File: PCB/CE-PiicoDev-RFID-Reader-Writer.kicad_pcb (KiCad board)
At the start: 2 copper layers, 25.4 x 52 mm, 63 parts, among them J1 , J2 , J3 Conn_01x06_Male, J4 Conn_01x01_Male, SW1 SW_DIP_x02, U1 MFRC522, Y1 27.12MHz 12pF

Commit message: v10 Release
Remove testpoints
Change ASW order so SW1 is LSB
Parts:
- removed TP1, TP2, TP3, TP4: TestPoint, CoreElectronics_Components:TestPoint_Pad_0.7x0.7mm
- moved R6 0.10 mm to (95.9, 109.8)
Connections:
- U1 pad 29: Net-(R7-Pad1) -> Net-(R6-Pad1)
- U1 pad 30: Net-(R6-Pad1) -> Net-(R7-Pad1)
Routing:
- net Net-(C3-Pad2): track 6.82 -> 4.16 mm, vias 1 -> 0
- net Net-(L2-Pad1): track 10.6 -> 8.78 mm, vias 3 -> 2
- net GND: track 35.1 -> 36.5 mm
- net Net-(R7-Pad1): track 16.7 -> 18.0 mm
- net Net-(C2-Pad2): track 7.86 -> 6.73 mm, vias 1 -> 0
- net Net-(L1-Pad1): vias 1 -> 0
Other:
- board text added: "0x2C 0x2D 0x2E 0x2F"
- board text added: "1 OFF ON OFF ON"
- board text added: "2 OFF OFF ON ON"
- board text added: "ASW"
- board text added: "RFID Module"
- board text added: "v10"
- board text removed: "RFID Reader Writer"
- board text removed: "v04"

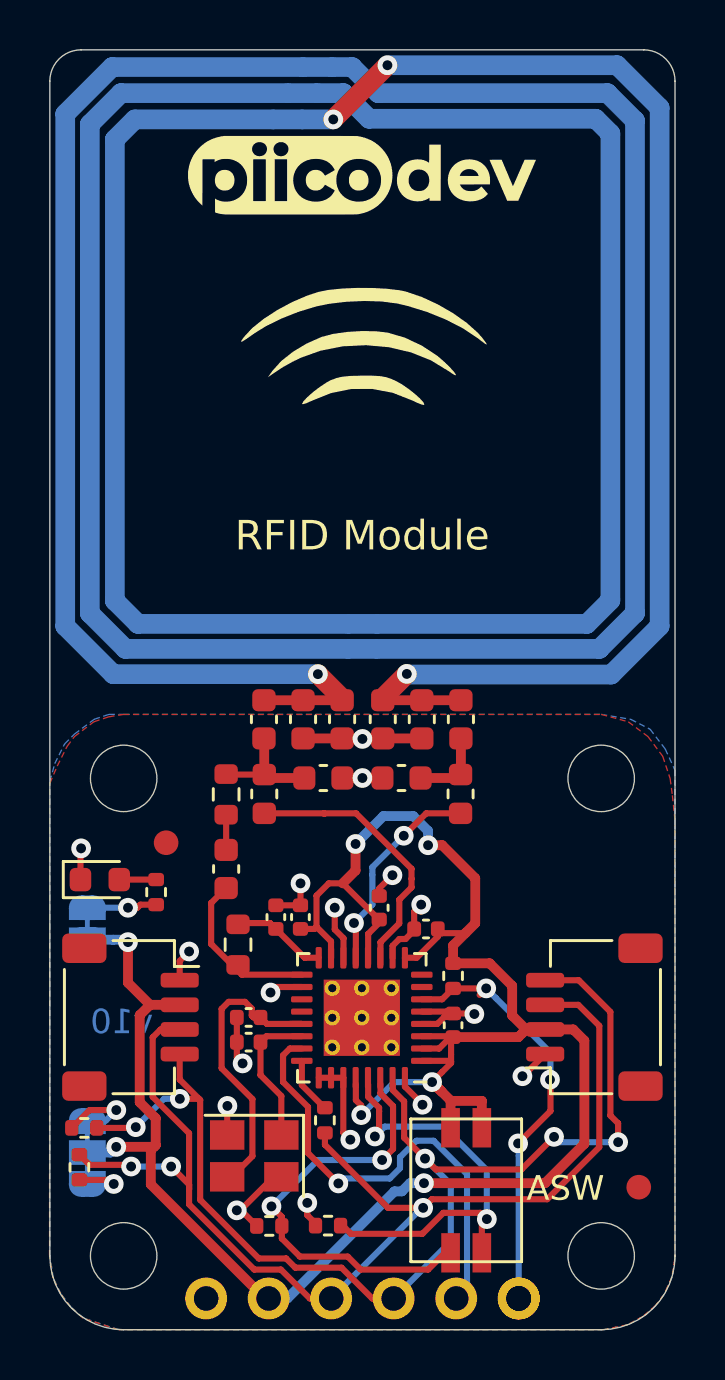
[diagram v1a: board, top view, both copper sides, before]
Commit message: Move coil down 0.2mm
Avoids issues with V-Cuts
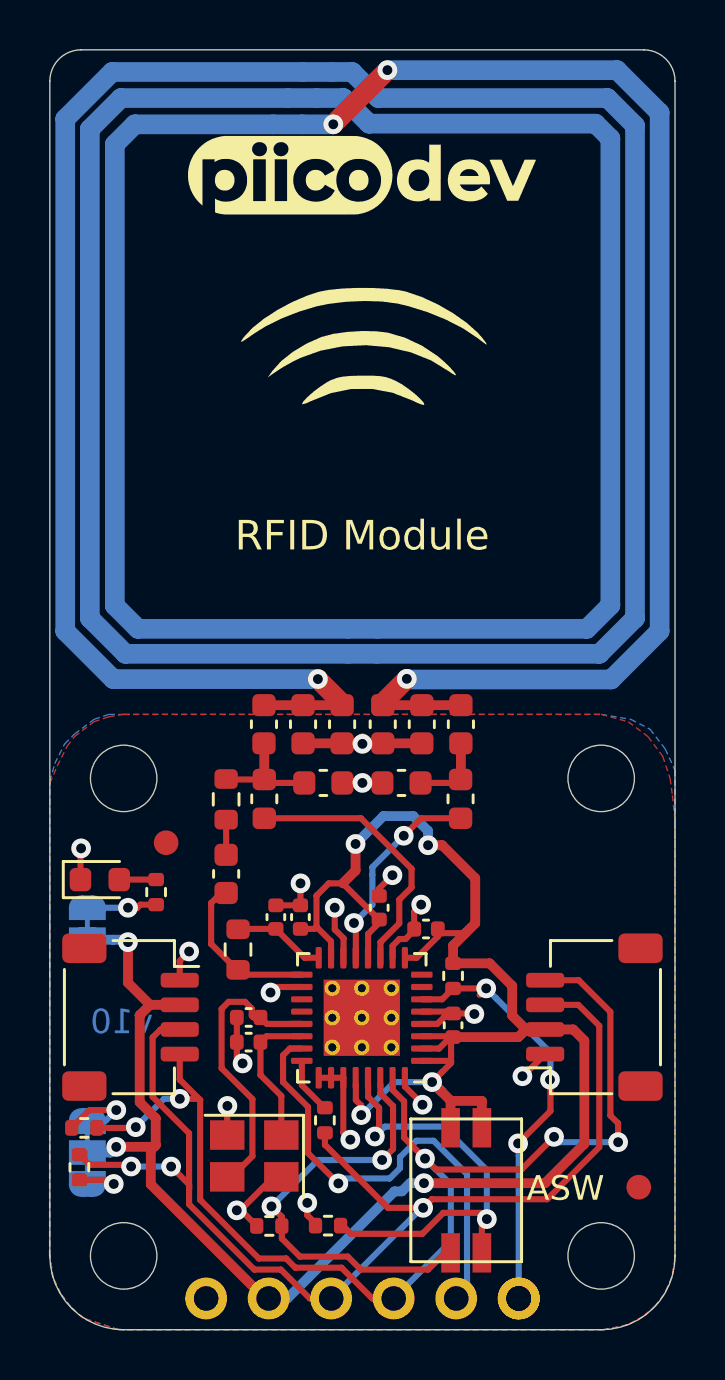
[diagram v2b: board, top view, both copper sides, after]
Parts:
- moved C10 0.20 mm to (99.7, 89.4)
- moved C15 0.20 mm to (96.5, 89.4)
- moved C16 0.20 mm to (98.1, 89.4)
- moved C2 0.20 mm to (91.7, 95.5)
- moved C5 0.20 mm to (95.7, 91.8)
- moved C6 0.20 mm to (98.9, 91.8)
- moved C7 0.20 mm to (93.3, 89.4)
- moved C8 0.20 mm to (101.3, 89.4)
- moved C9 0.20 mm to (94.9, 89.4)
- moved L1 0.20 mm to (93.3, 92.5)
- moved L2 0.20 mm to (101.3, 92.5)
- moved NT10 0.20 mm to (97.3, 85.6)
- moved NT11 0.20 mm to (94.2, 65.1)
- moved NT4 0.20 mm to (97.3, 86.6)
- moved NT9 0.20 mm to (94.8, 64.0)
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
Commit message: Change R5 to 1k
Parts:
- R5: value 470R -> 1k
